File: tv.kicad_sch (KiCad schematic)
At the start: 43 parts, among them IC1 CXA1145, IC29 74HC4024, IC30 74HC10, U1 Analog Video breakout, X1 4.433619MHz

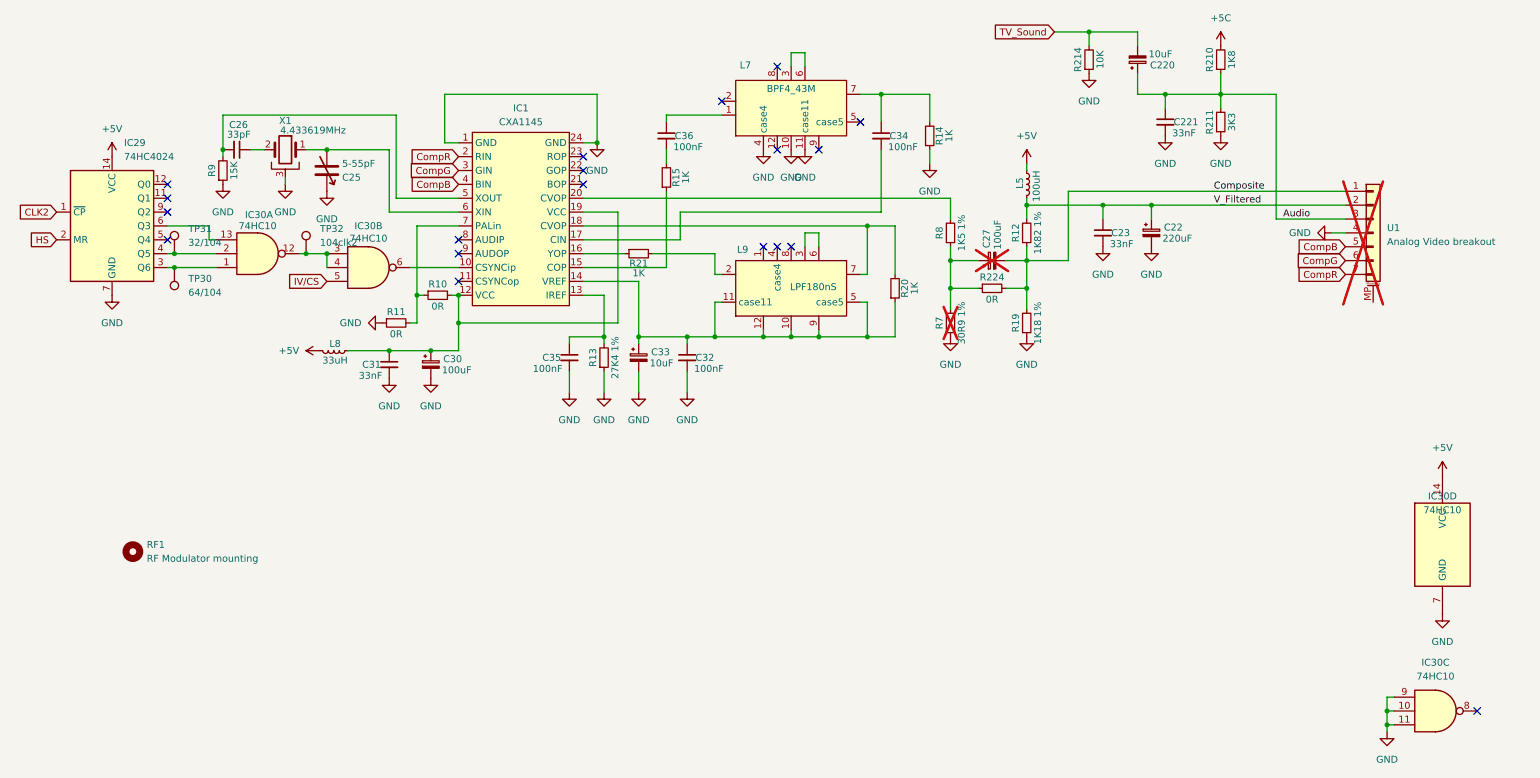
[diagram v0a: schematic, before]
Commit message: add ide and rework onboard ram
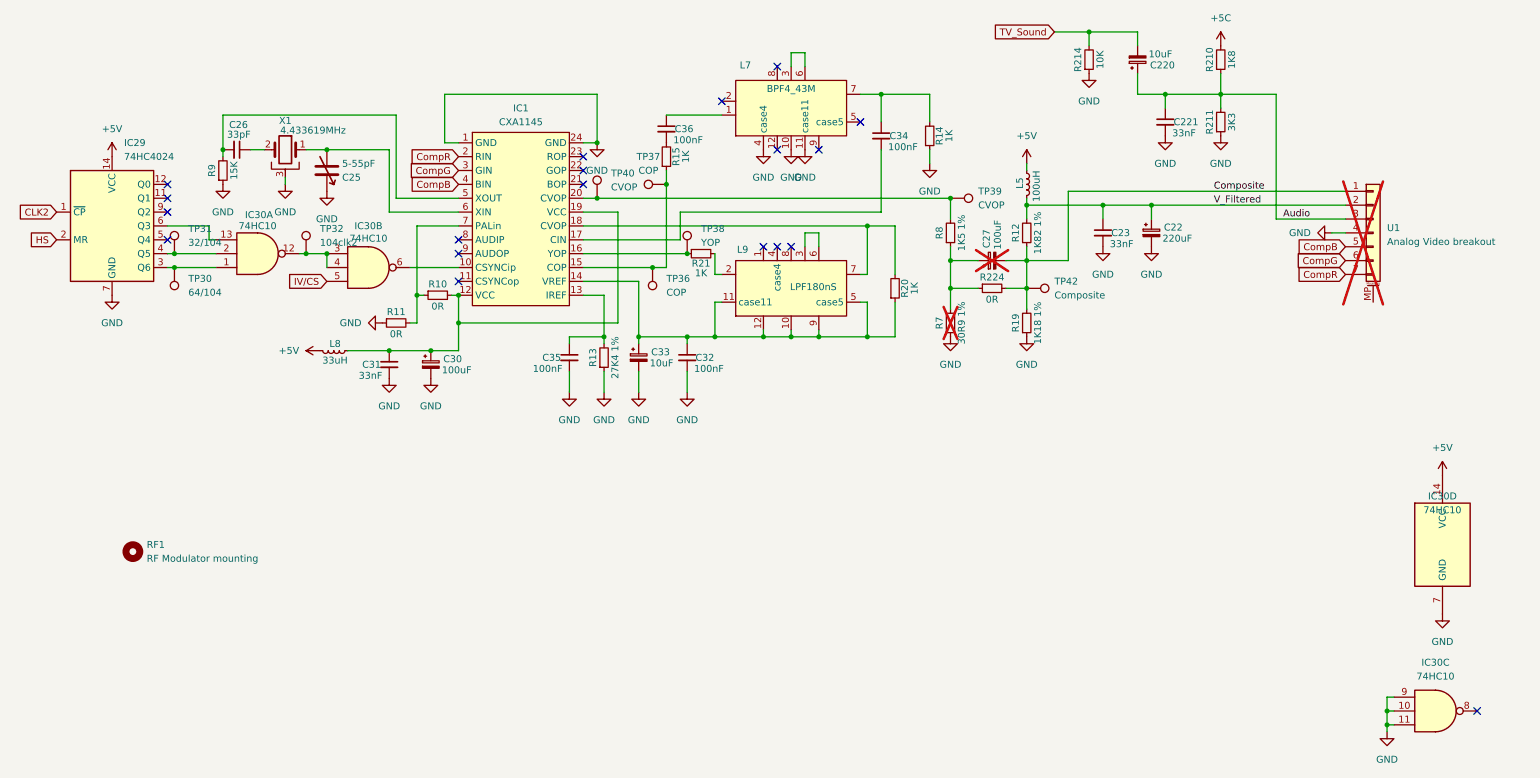
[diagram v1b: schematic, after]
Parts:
- added TP36, TP37: COP, TestPoint:TestPoint_Pad_D1.0mm, symbol Connector:TestPoint
- added TP38: YOP, TestPoint:TestPoint_Pad_D1.0mm, symbol Connector:TestPoint
- added TP39, TP40: CVOP, TestPoint:TestPoint_Pad_D1.0mm, symbol Connector:TestPoint
- added TP42: Composite, TestPoint:TestPoint_Pad_D1.0mm, symbol Connector:TestPoint
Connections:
- net Composite: now also TP42.1
- net at IC1.20 (CVOP), R8.2: now also TP39.1, TP40.1
- net at IC1.15 (COP), R15.1: now also TP36.1, TP37.1
- net at IC1.16 (YOP), R21.1: now also TP38.1
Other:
- moved on the sheet: C36, R15, R21
